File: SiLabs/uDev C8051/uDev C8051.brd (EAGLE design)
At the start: 22.9 x 15.2 mm, 17 parts, among them SW1 SPST.B3U-1000P(M), U1 C8051F387, U2 IP4221CZ6-S

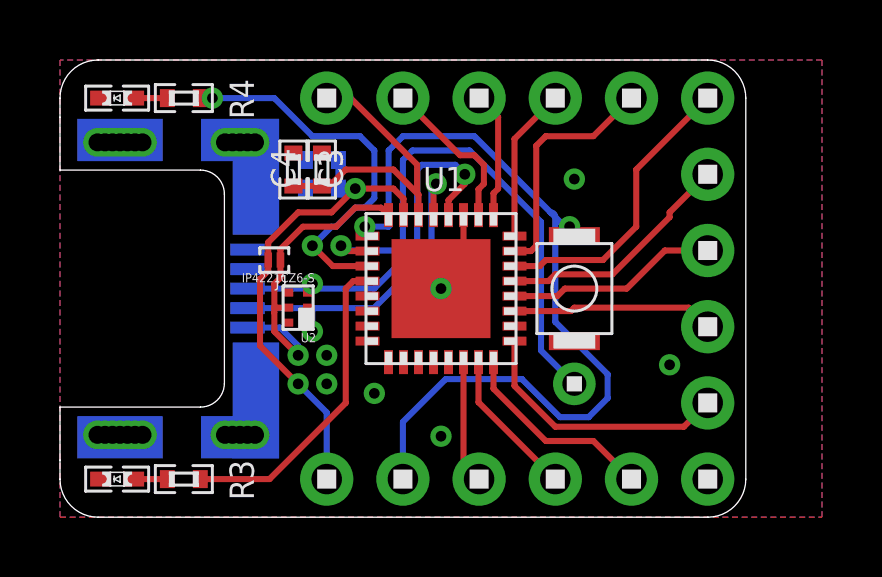
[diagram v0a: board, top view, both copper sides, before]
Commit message: Completed uDev C8051 PCB (tiny as FUCK) Renamed files from F287 Trinket to uDev C8051
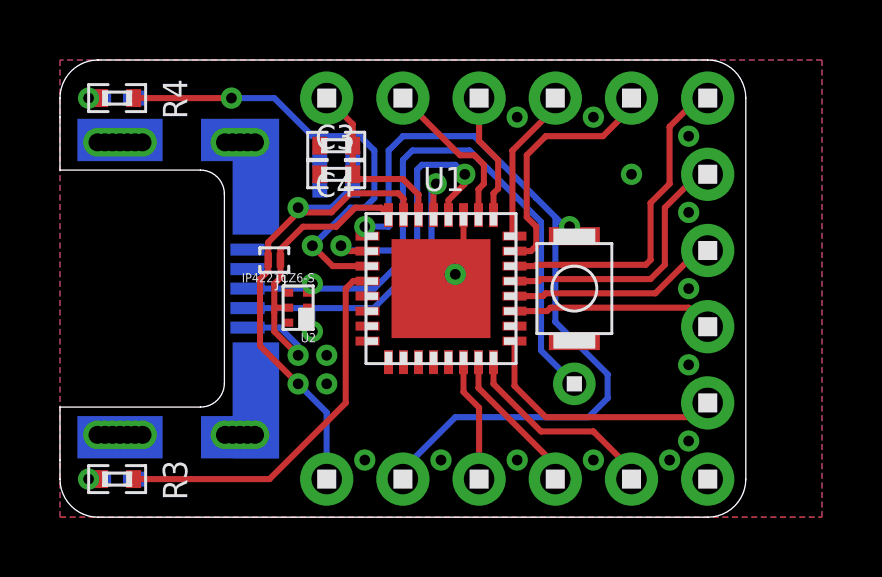
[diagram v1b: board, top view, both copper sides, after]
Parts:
- U1: value C8051F387 -> C8051F381/3/57
- moved R3 2.22 mm to (1.91, 1.27)
- moved R4 2.22 mm to (1.91, 14.0)
- moved C3 1.44 mm to (9.21, 11.4), turned to 180 degrees
- moved C4 0.93 mm to (9.21, 12.4), turned to 180 degrees
- moved C1 0.48 mm to (9.21, 11.0)
- moved C2 0.48 mm to (9.21, 11.9)
- flipped D1 to the bottom
- flipped D2 to the bottom
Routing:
- net 3.3V: track 10.3 -> 6.05 mm
- net P2.6: track 10.5 -> 12.8 mm
- net P2.7: track 12.9 -> 15.2 mm
- net !RST: track 28.6 -> 26.4 mm
- net VIN: track 16.4 -> 17.9 mm
- net P0.4: track 9.88 -> 11.0 mm
- net P0.5: track 8.01 -> 9.03 mm
- net GND: track 2.76 -> 2.09 mm, vias 7 -> 16
- net N$2: track 1.12 -> 0.80 mm, vias 0 -> 1
- net N$1: track 1.12 -> 0.80 mm, vias 0 -> 1
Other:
- board text added: "!RST!"
- board text added: "0.4 0.5 0.6 0.7 1.1 GND"
- board text added: "2.6"
- board text added: "2.7"
- board text added: "3.3v 0.0 0.1 0.2 0.3"
- board text added: "Vin !RST! 1.4 1.3 1.2"
- board text added: "uDev C8051"
- board text removed: "!RST"
- board text removed: "3.3v"
- board text removed: "5v"
- board text removed: "C2D"
- board text removed: "F387 uDev"
- board text removed: "GND"
- board text removed: "P0.0"
- board text removed: "P0.1"
- board text removed: "P0.2"
- board text removed: "P0.3"
- board text removed: "P0.4"
- board text removed: "P0.5"
- board text removed: "P0.6"
- board text removed: "P0.7"
- board text removed: "P1.0"
- board text removed: "P1.1"
